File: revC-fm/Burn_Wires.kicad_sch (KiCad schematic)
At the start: 14 parts, among them K1 PE014006, Q29 MMDT5551-7-F, Q51 BSZ180P03NS3GATMA1, Q52 MMBT2222LT1G, Q54 BSZ180P03NS3GATMA1

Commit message: working revC
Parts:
- D9: Mfr. Part No (none) -> SBRT5A50SA-13
- Q34: renamed from Q51; Mfr. Part No (none) -> BSZ180P03NS3GATMA1
- Q37: renamed from Q54; Mfr. Part No (none) -> BSZ180P03NS3GATMA1
- R125: renamed from R194; footprint Resistor_SMD:R_0603_1608Metric -> Resistor_SMD:R_0402_1005Metric
- R126: renamed from R195; footprint Resistor_SMD:R_0603_1608Metric -> Resistor_SMD:R_0402_1005Metric
- R127: renamed from R196; footprint Resistor_SMD:R_0603_1608Metric -> Resistor_SMD:R_0402_1005Metric
- R128: renamed from R197; footprint Resistor_SMD:R_0603_1608Metric -> Resistor_SMD:R_0402_1005Metric
- R129: renamed from R198; footprint Resistor_SMD:R_0603_1608Metric -> Resistor_SMD:R_0402_1005Metric
- R130: renamed from R199; footprint Resistor_SMD:R_0603_1608Metric -> Resistor_SMD:R_0402_1005Metric
- R131: renamed from R200; footprint Resistor_SMD:R_0603_1608Metric -> Resistor_SMD:R_0402_1005Metric
- renumbered Q52 to Q35

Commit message: working
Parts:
- renumbered Q34 to Q20, Q35 to Q21, Q37 to Q23, R130 to R100, R131 to R101, R125 to R95, R126 to R96, R127 to R97, R128 to R98, R129 to R99
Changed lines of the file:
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@@
   (symbol (lib_id "Device:R_US") (at 158.75 81.28 270) (unit 1)
     (in_bom yes) (on_board yes) (dnp no)
-    (property "Reference" "R131" (at 159.766 85.852 90)
+    (property "Reference" "R101" (at 159.766 85.852 90)
       (effects (font (size 1.27 1.27)) (justify bottom))
     )
@@
       (project "mainboard"
         (path "/d1441985-7b63-4bf8-a06d-c70da2e3b78b/00000000-0000-0000-0000-00005cec6476"
-          (reference "R131") (unit 1)
+          (reference "R101") (unit 1)
         )
       )
@@
   (symbol (lib_id "Device:R_US") (at 45.72 47.625 90) (unit 1)
     (in_bom yes) (on_board yes) (dnp no)
-    (property "Reference" "R127" (at 41.91 43.18 90)
+    (property "Reference" "R97" (at 41.91 43.18 90)
       (effects (font (size 1.27 1.27)) (justify right))
     )
@@
       (project "mainboard"
         (path "/d1441985-7b63-4bf8-a06d-c70da2e3b78b/00000000-0000-0000-0000-00005cec6476"
-          (reference "R127") (unit 1)
+          (reference "R97") (unit 1)
         )
       )
@@
   (symbol (lib_id "Device:R_US") (at 185.42 73.025 90) (unit 1)
     (in_bom yes) (on_board yes) (dnp no)
-    (property "Reference" "R130" (at 194.945 69.85 90)
+    (property "Reference" "R100" (at 194.945 69.85 90)
       (effects (font (size 1.27 1.27)) (justify bottom))
     )
@@
       (project "mainboard"
         (path "/d1441985-7b63-4bf8-a06d-c70da2e3b78b/00000000-0000-0000-0000-00005cec6476"
-          (reference "R130") (unit 1)
+          (reference "R100") (unit 1)
         )
       )
@@
   (symbol (lib_id "SierraLobo:BSZ086") (at 190.5 30.48 270) (mirror x) (unit 1)
     (in_bom yes) (on_board yes) (dnp no)
-    (property "Reference" "Q34" (at 187.96 22.86 90)
+    (property "Reference" "Q20" (at 187.96 22.86 90)
       (effects (font (size 1.27 1.27)) (justify left bottom))
     )
@@
       (project "mainboard"
         (path "/d1441985-7b63-4bf8-a06d-c70da2e3b78b/00000000-0000-0000-0000-00005cec6476"
-          (reference "Q34") (unit 1)
+          (reference "Q20") (unit 1)
         )
       )
@@
   (symbol (lib_id "SierraLobo:BSZ086") (at 190.5 60.96 270) (mirror x) (unit 1)
     (in_bom yes) (on_board yes) (dnp no)
-    (property "Reference" "Q37" (at 186.69 53.34 90)
+    (property "Reference" "Q23" (at 186.69 53.34 90)
       (effects (font (size 1.27 1.27)) (justify left bottom))
     )
@@
       (project "mainboard"
         (path "/d1441985-7b63-4bf8-a06d-c70da2e3b78b/00000000-0000-0000-0000-00005cec6476"
-          (reference "Q37") (unit 1)
+          (reference "Q23") (unit 1)
         )
       )
@@
   (symbol (lib_id "Device:Q_NPN_BEC") (at 55.88 47.625 0) (unit 1)
     (in_bom yes) (on_board yes) (dnp no)
-    (property "Reference" "Q35" (at 62.23 46.355 0)
+    (property "Reference" "Q21" (at 62.23 46.355 0)
       (effects (font (size 1.27 1.27)) (justify left))
     )
@@
       (project "mainboard"
         (path "/d1441985-7b63-4bf8-a06d-c70da2e3b78b/00000000-0000-0000-0000-00005cec6476"
-          (reference "Q35") (unit 1)
+          (reference "Q21") (unit 1)
         )
       )
@@
   (symbol (lib_id "Device:R_US") (at 186.055 41.91 90) (unit 1)
     (in_bom yes) (on_board yes) (dnp no)
-    (property "Reference" "R126" (at 194.945 42.037 90)
+    (property "Reference" "R96" (at 194.945 42.037 90)
       (effects (font (size 1.27 1.27)) (justify bottom))
     )
@@
       (project "mainboard"
         (path "/d1441985-7b63-4bf8-a06d-c70da2e3b78b/00000000-0000-0000-0000-00005cec6476"
-          (reference "R126") (unit 1)
+          (reference "R96") (unit 1)
         )
       )
@@
   (symbol (lib_id "Device:R_US") (at 158.75 48.26 270) (unit 1)
     (in_bom yes) (on_board yes) (dnp no)
-    (property "Reference" "R128" (at 159.385 52.07 90)
+    (property "Reference" "R98" (at 159.385 52.07 90)
       (effects (font (size 1.27 1.27)) (justify bottom))
     )
@@
       (project "mainboard"
         (path "/d1441985-7b63-4bf8-a06d-c70da2e3b78b/00000000-0000-0000-0000-00005cec6476"
-          (reference "R128") (unit 1)
+          (reference "R98") (unit 1)
         )
       )
@@
   (symbol (lib_id "Device:R_US") (at 170.18 35.56 180) (unit 1)
     (in_bom yes) (on_board yes) (dnp no)
-    (property "Reference" "R125" (at 175.26 32.385 0)
+    (property "Reference" "R95" (at 175.26 32.385 0)
       (effects (font (size 1.27 1.27)) (justify bottom))
     )
@@
       (project "mainboard"
         (path "/d1441985-7b63-4bf8-a06d-c70da2e3b78b/00000000-0000-0000-0000-00005cec6476"
-          (reference "R125") (unit 1)
+          (reference "R95") (unit 1)
         )
       )
@@
   (symbol (lib_id "Device:R_US") (at 170.18 66.04 180) (unit 1)
     (in_bom yes) (on_board yes) (dnp no)
-    (property "Reference" "R129" (at 175.26 63.5 0)
+    (property "Reference" "R99" (at 175.26 63.5 0)
       (effects (font (size 1.27 1.27)) (justify bottom))
     )
@@
       (project "mainboard"
         (path "/d1441985-7b63-4bf8-a06d-c70da2e3b78b/00000000-0000-0000-0000-00005cec6476"
-          (reference "R129") (unit 1)
+          (reference "R99") (unit 1)
         )
       )
@@
   (symbol (lib_id "power:GND") (at 104.14 38.1 0) (unit 1)
     (in_bom yes) (on_board yes) (dnp no)
-    (property "Reference" "#PWR0120" (at 104.14 44.45 0)
+    (property "Reference" "#PWR0106" (at 104.14 44.45 0)
       (effects (font (size 1.27 1.27)) hide)
     )
@@
       (project "mainboard"
         (path "/d1441985-7b63-4bf8-a06d-c70da2e3b78b/00000000-0000-0000-0000-00005cec6476"
-          (reference "#PWR0120") (unit 1)
+          (reference "#PWR0106") (unit 1)
         )
       )
@@
   (symbol (lib_id "power:GND") (at 170.18 53.34 0) (unit 1)
     (in_bom yes) (on_board yes) (dnp no)
-    (property "Reference" "#PWR0121" (at 170.18 59.69 0)
+    (property "Reference" "#PWR0107" (at 170.18 59.69 0)
       (effects (font (size 1.27 1.27)) hide)
     )
@@
       (project "mainboard"
         (path "/d1441985-7b63-4bf8-a06d-c70da2e3b78b/00000000-0000-0000-0000-00005cec6476"
-          (reference "#PWR0121") (unit 1)
+          (reference "#PWR0107") (unit 1)
         )
       )
@@
   (symbol (lib_id "power:GND") (at 58.42 55.88 0) (unit 1)
     (in_bom yes) (on_board yes) (dnp no)
-    (property "Reference" "#PWR0122" (at 58.42 62.23 0)
+    (property "Reference" "#PWR0108" (at 58.42 62.23 0)
       (effects (font (size 1.27 1.27)) hide)
     )
@@
       (project "mainboard"
         (path "/d1441985-7b63-4bf8-a06d-c70da2e3b78b/00000000-0000-0000-0000-00005cec6476"
-          (reference "#PWR0122") (unit 1)
+          (reference "#PWR0108") (unit 1)
         )
       )
@@
   (symbol (lib_id "power:GND") (at 170.18 86.36 0) (unit 1)
     (in_bom yes) (on_board yes) (dnp no)
-    (property "Reference" "#PWR0123" (at 170.18 92.71 0)
+    (property "Reference" "#PWR0109" (at 170.18 92.71 0)
       (effects (font (size 1.27 1.27)) hide)
     )
@@
       (project "mainboard"
         (path "/d1441985-7b63-4bf8-a06d-c70da2e3b78b/00000000-0000-0000-0000-00005cec6476"
-          (reference "#PWR0123") (unit 1)
+          (reference "#PWR0109") (unit 1)
         )
       )
@@
         )
         (path "/d1441985-7b63-4bf8-a06d-c70da2e3b78b/00000000-0000-0000-0000-00005cec6476"
-          (reference "Q36") (unit 2)
+          (reference "Q22") (unit 2)
         )
       )
@@
         )
         (path "/d1441985-7b63-4bf8-a06d-c70da2e3b78b/00000000-0000-0000-0000-00005cec6476"
-          (reference "Q36") (unit 1)
+          (reference "Q22") (unit 1)
         )
       )
@@
         )
         (path "/d1441985-7b63-4bf8-a06d-c70da2e3b78b/00000000-0000-0000-0000-00005cec6476"
-          (reference "D1") (unit 1)
-        )
-      )
+          (reference "D4") (unit 1)
+        )
+      )

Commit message: almost done!!!!!
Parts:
- Q20, Q23: value BSZ180P03NS3GATMA1 -> BSZ180
- renumbered D9 to D4
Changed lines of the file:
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@@
       (effects (font (size 1.27 1.27)) (justify left bottom))
     )
-    (property "Value" "BSZ180P03NS3GATMA1" (at 198.12 26.67 90)
+    (property "Value" "BSZ180" (at 198.12 26.67 90)
       (effects (font (size 1.27 1.27)))
     )
@@
       (effects (font (size 1.27 1.27)) (justify left bottom))
     )
-    (property "Value" "BSZ180P03NS3GATMA1" (at 198.12 57.15 90)
+    (property "Value" "BSZ180" (at 198.12 57.15 90)
       (effects (font (size 1.27 1.27)))
     )
@@
   (symbol (lib_id "mainboard-rescue:D_Schottky-Device-mainboard-rescue") (at 58.42 34.29 270) (unit 1)
     (in_bom yes) (on_board yes) (dnp no)
-    (property "Reference" "D9" (at 58.42 27.7114 90)
+    (property "Reference" "D4" (at 58.42 27.7114 90)
       (effects (font (size 1.27 1.27)))
     )
@@
     (instances
       (project "mainboard"
-        (path "/d1441985-7b63-4bf8-a06d-c70da2e3b78b/00000000-0000-0000-0000-00005cec5dde/a78437db-a0fc-4cde-8346-4d17e2576807"
-          (reference "D9") (unit 1)
-        )
         (path "/d1441985-7b63-4bf8-a06d-c70da2e3b78b/00000000-0000-0000-0000-00005cec6476"
           (reference "D4") (unit 1)

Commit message: updated fab files
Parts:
- D10: renamed from D4; value SBRT5A50SA-13 -> B260S1F-7; footprint Diode_SMD:D_SMA -> Diode_SMD:D_SOD-123F; Manufacturer (none) -> Diodes Incorporated; Mfr. Part No SBRT5A50SA-13 -> B260S1F-7
- K1: Manufacturer (none) -> TE Connectivity; Mfr. Part No (none) -> PE014006
- Q29: Manufacturer (none) -> Diodes Incorporated; Mfr. Part No (none) -> MMDT5551-7-F
- Q62: renamed from Q20; Manufacturer (none) -> Infineon
- Q63: renamed from Q21; value MMBT2222LT1G -> IRLML2803; symbol Device:Q_NPN_BEC -> Device:Q_NMOS_GSD; Manufacturer (none) -> Infineon; Mfr. Part No (none) -> IRLML2803TRPBF
- Q65: renamed from Q23; Manufacturer (none) -> Infineon
- R255: renamed from R95; Manufacturer (none) -> Stackpole Electronics; Mfr. Part No (none) -> RMCF0402FT100K
- R256: renamed from R96; Manufacturer (none) -> Panasonic; Mfr. Part No (none) -> ERJ-2GEJ102X
- R257: renamed from R97; Manufacturer (none) -> Panasonic; Mfr. Part No (none) -> ERJ-2GEJ102X
- R258: renamed from R98; Manufacturer (none) -> Stackpole Electronics; Mfr. Part No (none) -> RMCF0402FT100K
- R259: renamed from R99; Manufacturer (none) -> Stackpole Electronics; Mfr. Part No (none) -> RMCF0402FT100K
- R260: renamed from R100; Manufacturer (none) -> Panasonic; Mfr. Part No (none) -> ERJ-2GEJ102X
- R261: renamed from R101; Manufacturer (none) -> Stackpole Electronics; Mfr. Part No (none) -> RMCF0402FT100K
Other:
- note removed: "in a larger package than other NPN's due to temp. derating"

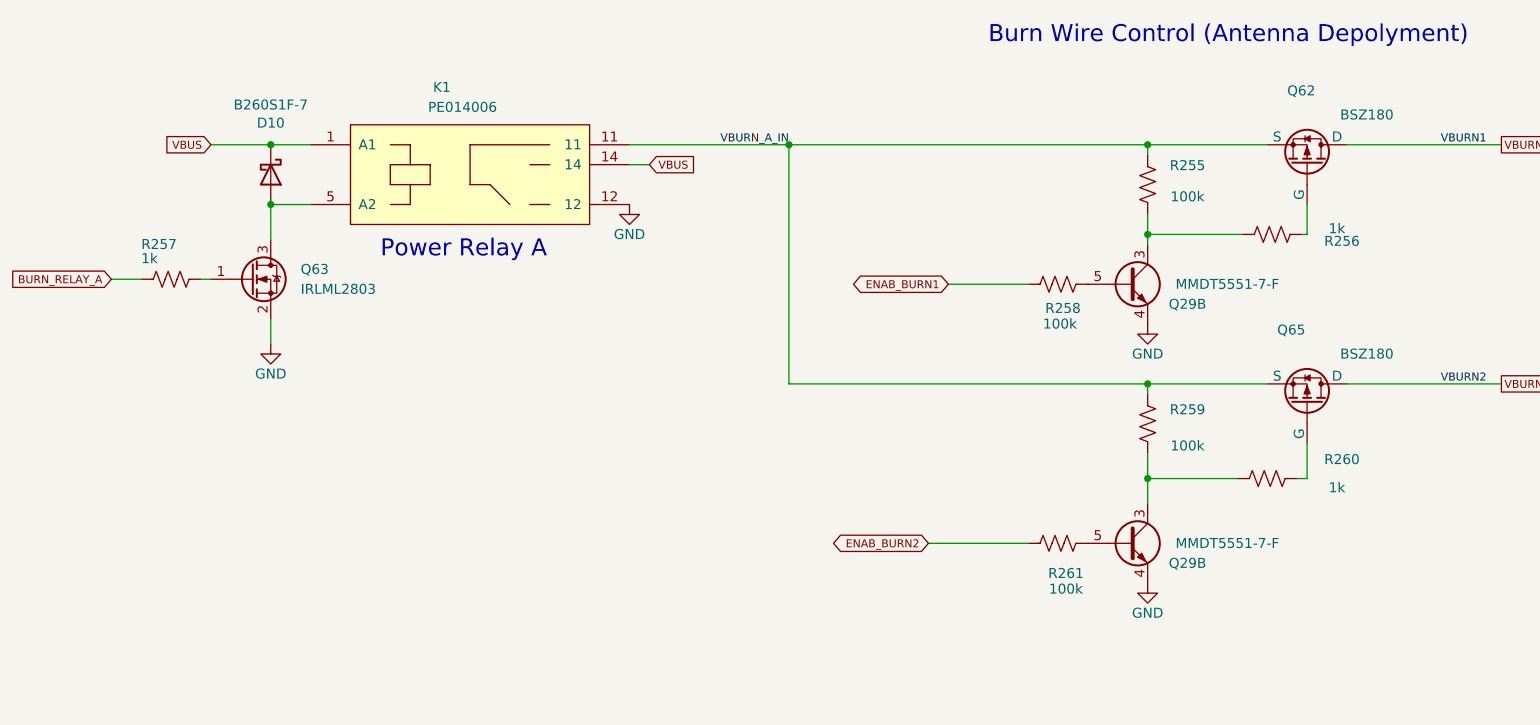
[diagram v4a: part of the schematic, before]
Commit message: updated per review, improved docs
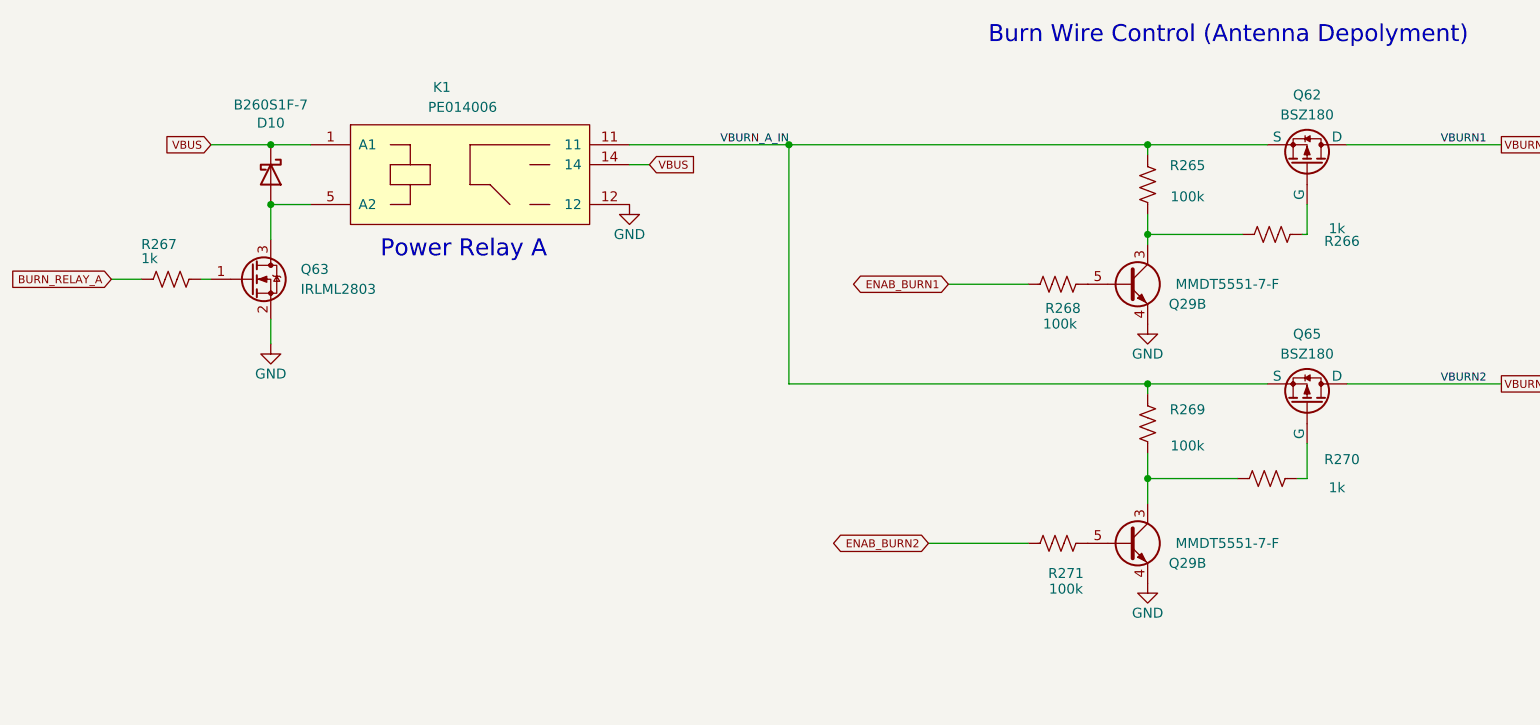
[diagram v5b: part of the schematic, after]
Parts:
- renumbered R255 to R265, R256 to R266, R257 to R267, R258 to R268, R259 to R269, R260 to R270, R261 to R271
